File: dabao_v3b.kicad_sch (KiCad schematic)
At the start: 45 parts, among them J1 USB_C_Receptacle_USB2.0_16P, SW1 SW_Push, SW2 SW_Push, U1 baochip1x, U3 Baochip, U4 MT3406, U5 EMS4000RSW, U6 MT3406, Y2 48.000MHz

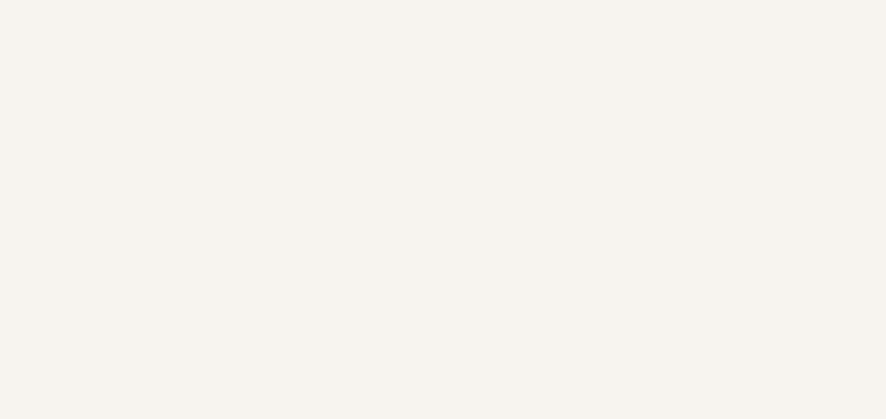
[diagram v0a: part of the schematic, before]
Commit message: add artifacts required for USB ID
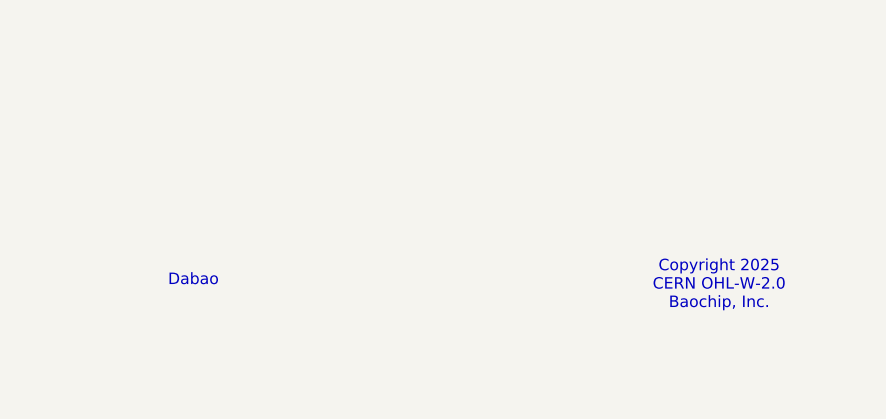
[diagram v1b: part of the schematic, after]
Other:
- note added: "Copyright 2025 CERN OHL-W-2.0 Baochip, Inc."
- note added: "Dabao"
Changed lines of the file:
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@@
+		)
+	)
+	(text "Copyright 2025\nCERN OHL-W-2.0\nBaochip, Inc."
+		(exclude_from_sim no)
+		(at 386.588 261.62 0)
+		(effects
+			(font
+				(size 1.27 1.27)
+			)
+		)
+	)
+	(text "Dabao"
+		(exclude_from_sim no)
+		(at 328.168 261.112 0)
+		(effects
+			(font
+				(size 1.27 1.27)
+			)
 		)
 	)
